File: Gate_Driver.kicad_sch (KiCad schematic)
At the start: 27 parts, among them U1 DRV8323RSRGZR

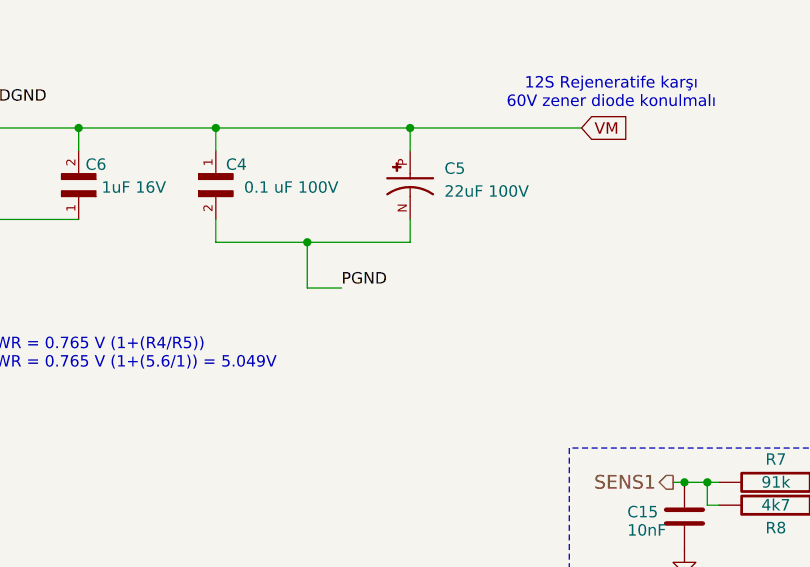
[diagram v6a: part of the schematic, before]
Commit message: Some pcb design and schematics editings about PGND_DRV
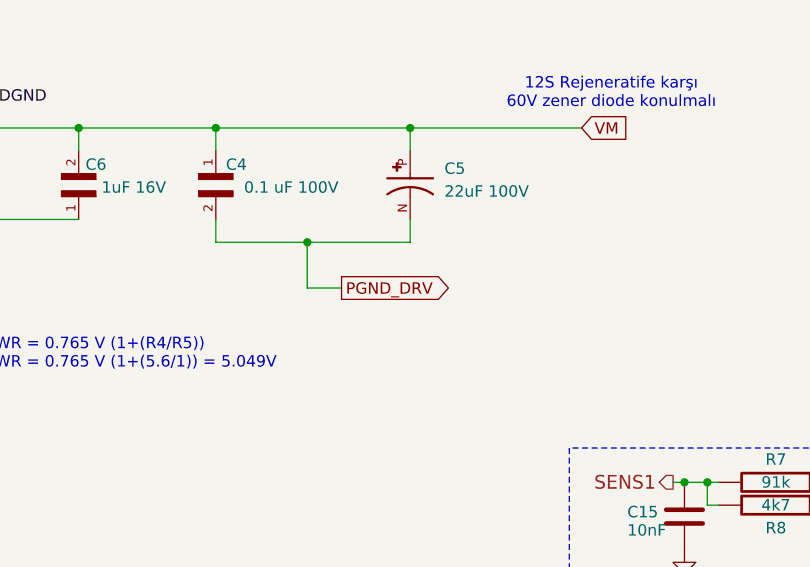
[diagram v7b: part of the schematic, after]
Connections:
- net PGND: no longer C4.2, C5.N
- new net PGND_DRV: C4.2, C5.N
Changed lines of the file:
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@@
-	)
-	(label "PGND"
-		(at 203.2 67.31 0)
-		(effects
-			(font
-				(size 1.27 1.27)
-			)
-			(justify left bottom)
-		)
 	)
 	(label "PGND"
@@
 		)
 	)
+	(global_label "PGND_DRV"
+		(shape output)
+		(at 203.2 67.31 0)
+		(fields_autoplaced yes)
+		(effects
+			(font
+				(size 1.27 1.27)
+			)
+			(justify left)
+		)
+		(property "Intersheetrefs" "${INTERSHEET_REFS}"
+			(at 215.9219 67.31 0)
+			(effects
+				(font
+					(size 1.27 1.27)
+				)
+				(justify left)
+				(hide yes)
+			)
+		)
+	)

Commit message: all routed pcb
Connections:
- net AGND is gone; now on net GND: C2.2, U1.35 (AGND)
- net BGND is gone; now on net GND: C3.1, U1.43 (BGND)
- net DGND is gone; now on net GND: C14.1, U1.27 (DGND)
- net PGND is gone; now on net GND: U1.2 (PGND)
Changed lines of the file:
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@@
 	)
 	(junction
+		(at 151.13 143.51)
+		(diameter 0)
+		(color 0 0 0 0)
+	)
+	(junction
 		(at 97.79 36.83)
 		(diameter 0)
@@
 	)
 	(junction
+		(at 151.13 138.43)
+		(diameter 0)
+		(color 0 0 0 0)
+	)
+	(junction
 		(at 241.3 104.14)
 		(diameter 0)
@@
 	)
 	(junction
+		(at 151.13 140.97)
+		(diameter 0)
+		(color 0 0 0 0)
+	)
+	(junction
 		(at 132.08 71.12)
 		(diameter 0)
@@
 	(wire
 		(pts
+			(xy 152.4 135.89) (xy 151.13 135.89)
+		)
+		(stroke
+			(width 0)
+			(type default)
+		)
+	)
+	(wire
+		(pts
 			(xy 245.11 119.38) (xy 243.84 119.38)
 		)
@@
 	(wire
 		(pts
+			(xy 151.13 143.51) (xy 151.13 144.78)
+		)
+		(stroke
+			(width 0)
+			(type default)
+		)
+	)
+	(wire
+		(pts
 			(xy 264.16 91.44) (xy 264.16 92.71)
 		)
@@
 	(wire
 		(pts
+			(xy 151.13 140.97) (xy 151.13 143.51)
+		)
+		(stroke
+			(width 0)
+			(type default)
+		)
+	)
+	(wire
+		(pts
 			(xy 48.26 69.85) (xy 52.07 69.85)
 		)
@@
 	(wire
 		(pts
+			(xy 151.13 140.97) (xy 152.4 140.97)
+		)
+		(stroke
+			(width 0)
+			(type default)
+		)
+	)
+	(wire
+		(pts
 			(xy 48.26 87.63) (xy 52.07 87.63)
 		)
@@
 	(wire
 		(pts
+			(xy 151.13 143.51) (xy 152.4 143.51)
+		)
+		(stroke
+			(width 0)
+			(type default)
+		)
+	)
+	(wire
+		(pts
 			(xy 243.84 116.84) (xy 245.11 116.84)
 		)
@@
 	(wire
 		(pts
+			(xy 151.13 138.43) (xy 151.13 140.97)
+		)
+		(stroke
+			(width 0)
+			(type default)
+		)
+	)
+	(wire
+		(pts
 			(xy 48.26 92.71) (xy 52.07 92.71)
 		)
@@
 	(wire
 		(pts
+			(xy 151.13 138.43) (xy 152.4 138.43)
+		)
+		(stroke
+			(width 0)
+			(type default)
+		)
+	)
+	(wire
+		(pts
 			(xy 241.3 88.9) (xy 243.84 88.9)
 		)
@@
 	(wire
 		(pts
+			(xy 151.13 135.89) (xy 151.13 138.43)
+		)
+		(stroke
+			(width 0)
+			(type default)
+		)
+	)
+	(wire
+		(pts
 			(xy 48.26 77.47) (xy 52.07 77.47)
 		)
@@
 	)
 	(label "BGND"
+		(at 152.4 135.89 0)
+		(effects
+			(font
+				(size 1.27 1.27)
+			)
+			(justify left bottom)
+		)
+	)
+	(label "BGND"
 		(at 144.78 44.45 0)
 		(effects
@@
 		)
 	)
+	(label "AGND"
+		(at 152.4 143.51 0)
+		(effects
+			(font
+				(size 1.27 1.27)
+			)
+			(justify left bottom)
+		)
+	)
+	(label "PGND"
+		(at 152.4 138.43 0)
+		(effects
+			(font
+				(size 1.27 1.27)
+			)
+			(justify left bottom)
+		)
+	)
 	(label "DGND"
 		(at 115.57 133.35 0)
@@
 		)
 	)
+	(label "DGND"
+		(at 152.4 140.97 0)
+		(effects
+			(font
+				(size 1.27 1.27)
+			)
+			(justify left bottom)
+		)
+	)
 	(global_label "PGND_DRV"
 		(shape output)
@@
 					(unit 1)
 				)
+			)
+		)
+	)
+	(symbol
+		(lib_id "power:GND")
+		(at 151.13 144.78 0)
+		(unit 1)
+		(exclude_from_sim no)
+		(in_bom yes)
+		(on_board yes)
+		(dnp no)
+		(fields_autoplaced yes)
+		(property "Reference" "#PWR059"
+			(at 151.13 151.13 0)
+			(effects
+				(font
+					(size 1.27 1.27)
+				)
+				(hide yes)
+			)
+		)
+		(property "Value" "GND"
+			(at 151.13 149.86 0)
+			(effects
+				(font
+					(size 1.27 1.27)
+				)
+			)
+		)
+		(property "Footprint" ""
+			(at 151.13 144.78 0)
+			(effects
+				(font
+					(size 1.27 1.27)
+				)
+				(hide yes)
+			)
+		)
+		(property "Datasheet" ""
+			(at 151.13 144.78 0)
+			(effects
+				(font
+					(size 1.27 1.27)
+				)
+				(hide yes)
+			)
+		)
+		(property "Description" "Power symbol creates a global label with name \"GND\" , ground"
+			(at 151.13 144.78 0)
+			(effects
+				(font
+					(size 1.27 1.27)
+				)
+				(hide yes)
+			)
+		)
+		(pin "1"
+		)
+		(instances
+			(project "Ana_ESC"
+				(path "/57129761-6d47-486c-bd7a-90dbb6f75754/beeab9ba-c868-48bf-b621-5886b9552033"
+					(reference "#PWR059")
+					(unit 1)
+				)
